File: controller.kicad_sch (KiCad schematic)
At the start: 26 parts, among them U4 STM32H742VGTx

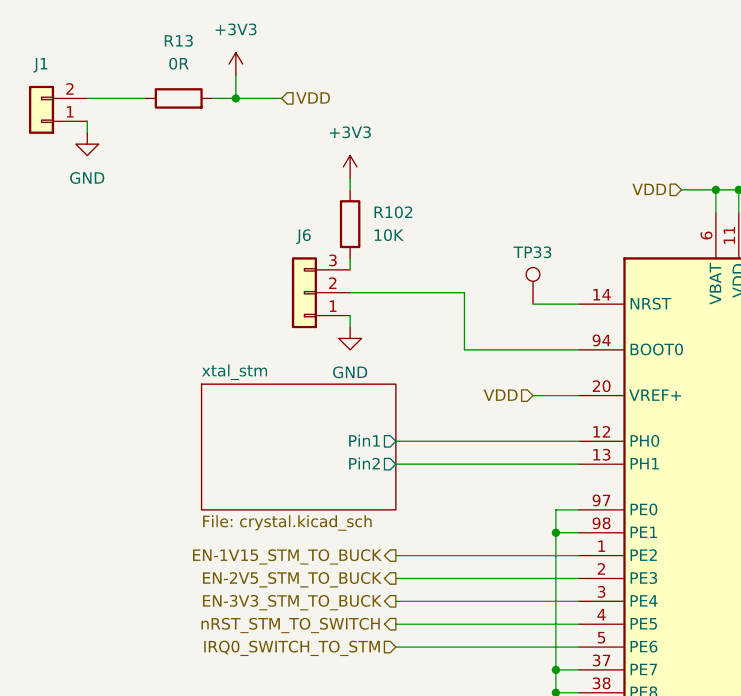
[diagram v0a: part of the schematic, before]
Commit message: moves +3V3 converter to root. Refs: #1
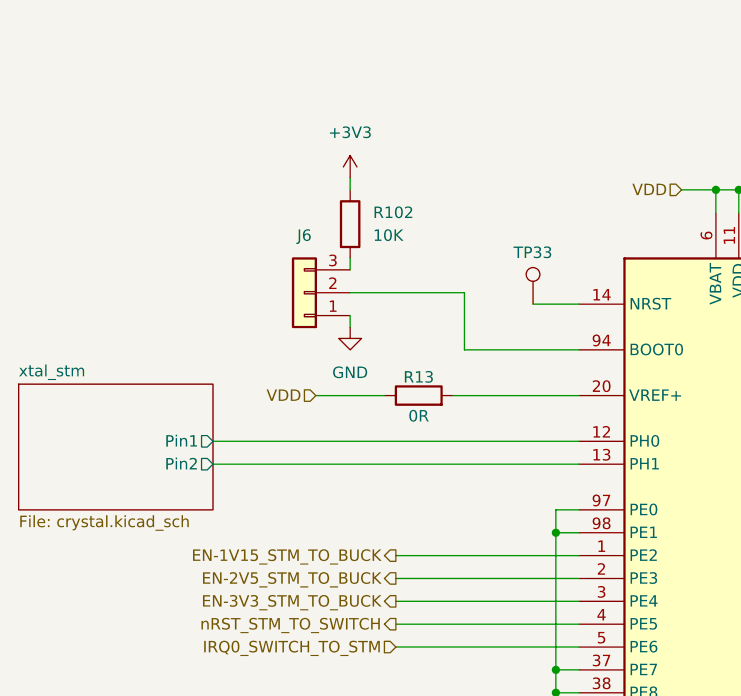
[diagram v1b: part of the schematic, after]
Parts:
- removed J1: ~, KL:02x01_2.54mm_Header, symbol KL_Headers:02x01_2.54mm_Header
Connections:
- net +3V3: no longer C70.1, C75.1, C76.1, C77.1, C78.1, C79.1, C80.1, C85.1, R13.2, U4.100 (VDD), U4.11 (VDD), U4.20 (VREF+), U4.21 (VDDA), U4.27 (VDD), U4.50 (VDD), U4.6 (VBAT), U4.75 (VDD)
- net VDD: now reaches R13.1
- net VDD: now also C70.1, C75.1, C76.1, C77.1, C78.1, C79.1, C80.1, C85.1, U4.100 (VDD), U4.11 (VDD), U4.21 (VDDA), U4.27 (VDD), U4.50 (VDD), U4.6 (VBAT), U4.75 (VDD)
- new net: R13.2, U4.20 (VREF+)
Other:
- moved on the sheet: R13

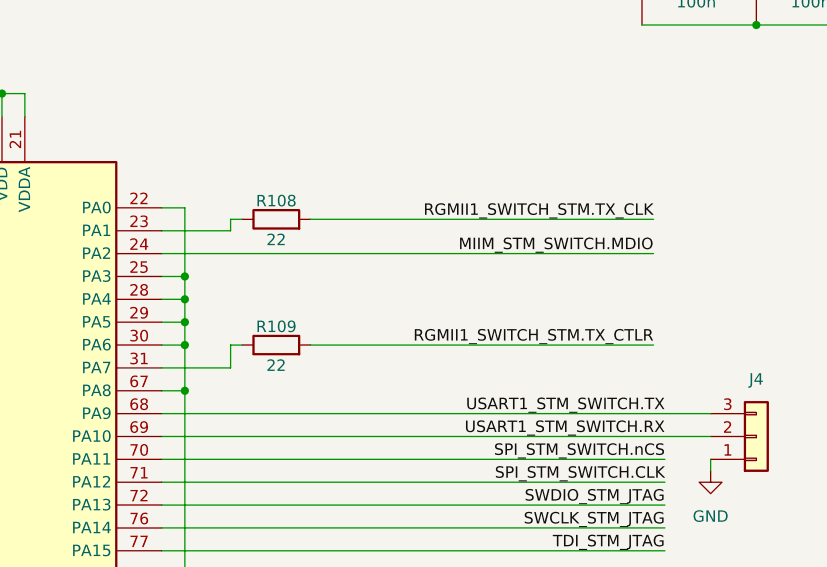
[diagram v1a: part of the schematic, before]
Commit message: fixes RGMII1 TX and RX resistors and duplicate name. Refs: #1
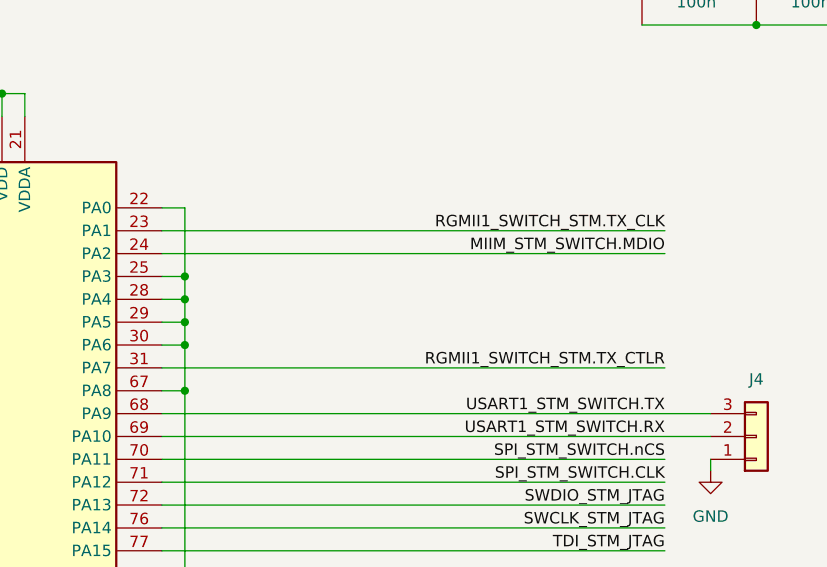
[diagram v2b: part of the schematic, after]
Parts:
- removed R108, R109: 22, KL_Footprints:R_0603, symbol KL_R:R_22_100mW_1pct_0603
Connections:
- net RGMII1_SWITCH_STM.TX_CLK: now also U4.23 (PA1)
- net RGMII1_SWITCH_STM.TX_CTLR: now also U4.31 (PA7)

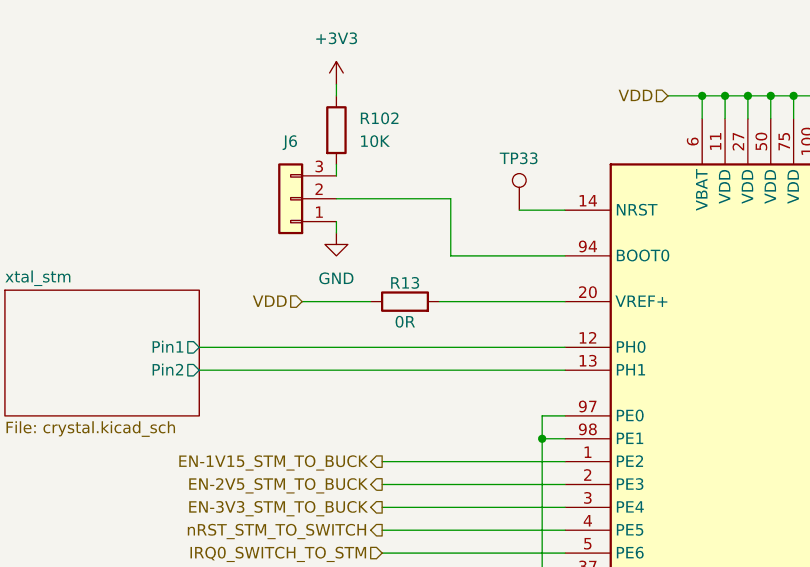
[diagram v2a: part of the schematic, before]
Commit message: fixes duplicate R13. Refs: #1
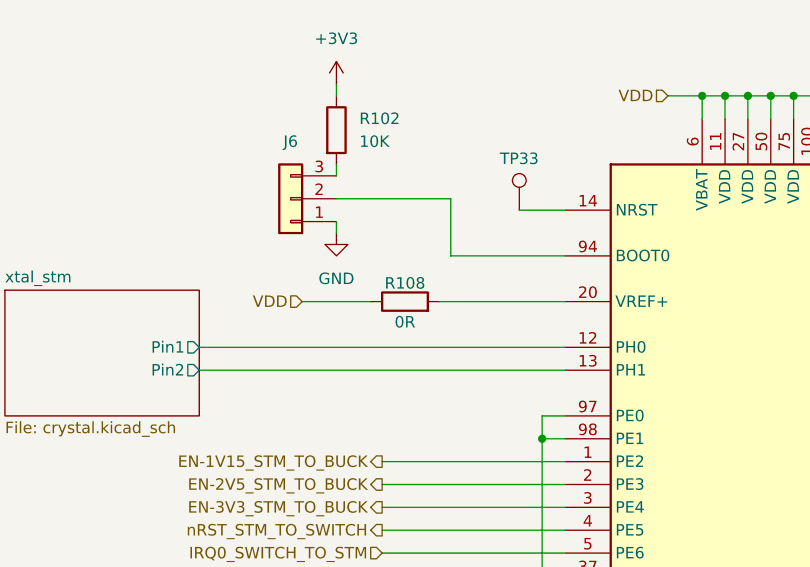
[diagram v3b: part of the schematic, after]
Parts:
- removed R13: 0R, KL_Footprints:R_2512, symbol KL_R:R_0R_2W_5_2512
- added R108: 0R, KL_Footprints:R_2512, symbol KL_R:R_0R_2W_5_2512
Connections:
- net VDD: now also R108.1
- net at U4.20 (VREF+): now also R108.2
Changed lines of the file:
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@@
-	)
-	(symbol
-		(lib_id "KL_R:R_0R_2W_5_2512")
-		(at 60.96 54.61 90)
-		(unit 1)
-		(exclude_from_sim no)
-		(in_bom yes)
-		(on_board yes)
-		(dnp no)
-		(property "Reference" "R13"
-			(at 60.96 52.578 90)
-			(effects
-				(font
-					(size 1.27 1.27)
-				)
-			)
-		)
-		(property "Value" "0R"
-			(at 60.96 56.896 90)
-			(effects
-				(font
-					(size 1.27 1.27)
-				)
-			)
-		)
-		(property "Footprint" "KL_Footprints:R_2512"
-			(at 60.96 56.388 90)
-			(effects
-				(font
-					(size 1.27 1.27)
-				)
-				(hide yes)
-			)
-		)
-		(property "Datasheet" "~"
-			(at 60.96 54.61 0)
-			(effects
-				(font
-					(size 1.27 1.27)
-				)
-				(hide yes)
-			)
-		)
-		(property "Description" "Resistor"
-			(at 60.96 54.61 0)
-			(effects
-				(font
-					(size 1.27 1.27)
-				)
-				(hide yes)
-			)
-		)
-		(property "Power" "2"
-			(at 60.96 54.61 0)
-			(effects
-				(font
-					(size 1.27 1.27)
-				)
-				(hide yes)
-			)
-		)
-		(property "Tolerance" "5"
-			(at 60.96 54.61 0)
-			(effects
-				(font
-					(size 1.27 1.27)
-				)
-				(hide yes)
-			)
-		)
-		(property "Mouser" "652-CRF2512-J-000ELF "
-			(at 60.96 54.61 0)
-			(effects
-				(font
-					(size 1.27 1.27)
-				)
-				(hide yes)
-			)
-		)
-		(property "Digikey" "118-CRF2512-J/-000ELFCT-ND"
-			(at 60.96 54.61 0)
-			(effects
-				(font
-					(size 1.27 1.27)
-				)
-				(hide yes)
-			)
-		)
-		(property "LCSC" "C2778666"
-			(at 60.96 54.61 0)
-			(effects
-				(font
-					(size 1.27 1.27)
-				)
-				(hide yes)
-			)
-		)
-		(pin "2"
-		)
-		(pin "1"
-		)
-		(instances
-			(project ""
-				(path "/d4536448-b109-4159-96e2-3dc21baf2d6e/06488c82-a47f-4277-b0ee-3bd211d8922a"
-					(reference "R13")
-					(unit 1)
-				)
-			)
-		)
 	)
 	(symbol
@@
 					(unit 1)
 				)
+			)
+		)
+	)
+	(symbol
+		(lib_id "KL_R:R_0R_2W_5_2512")
+		(at 60.96 54.61 90)
+		(unit 1)
+		(exclude_from_sim no)
+		(in_bom yes)
+		(on_board yes)
+		(dnp no)
+		(property "Reference" "R108"
+			(at 60.96 52.578 90)
+			(effects
+				(font
+					(size 1.27 1.27)
+				)
+			)
+		)
+		(property "Value" "0R"
+			(at 60.96 56.896 90)
+			(effects
+				(font
+					(size 1.27 1.27)
+				)
+			)
+		)
+		(property "Footprint" "KL_Footprints:R_2512"
+			(at 60.96 56.388 90)
+			(effects
+				(font
+					(size 1.27 1.27)
+				)
+				(hide yes)
+			)
+		)
+		(property "Datasheet" "~"
+			(at 60.96 54.61 0)
+			(effects
+				(font
+					(size 1.27 1.27)
+				)
+				(hide yes)
+			)
+		)
+		(property "Description" "Resistor"
+			(at 60.96 54.61 0)
+			(effects
+				(font
+					(size 1.27 1.27)
+				)
+				(hide yes)
+			)
+		)
+		(property "Power" "2"
+			(at 60.96 54.61 0)
+			(effects
+				(font
+					(size 1.27 1.27)
+				)
+				(hide yes)
+			)
+		)
+		(property "Tolerance" "5"
+			(at 60.96 54.61 0)
+			(effects
+				(font
+					(size 1.27 1.27)
+				)
+				(hide yes)
+			)
+		)
+		(property "Mouser" "652-CRF2512-J-000ELF "
+			(at 60.96 54.61 0)
+			(effects
+				(font
+					(size 1.27 1.27)
+				)
+				(hide yes)
+			)
+		)
+		(property "Digikey" "118-CRF2512-J/-000ELFCT-ND"
+			(at 60.96 54.61 0)
+			(effects
+				(font
+					(size 1.27 1.27)
+				)
+				(hide yes)
+			)
+		)
+		(property "LCSC" "C2778666"
+			(at 60.96 54.61 0)
+			(effects
+				(font
+					(size 1.27 1.27)
+				)
+				(hide yes)
+			)
+		)
+		(pin "2"
+		)
+		(pin "1"
+		)
+		(instances
+			(project "shish-lan"
+				(path "/d4536448-b109-4159-96e2-3dc21baf2d6e/06488c82-a47f-4277-b0ee-3bd211d8922a"
+					(reference "R108")
+					(unit 1)
+				)

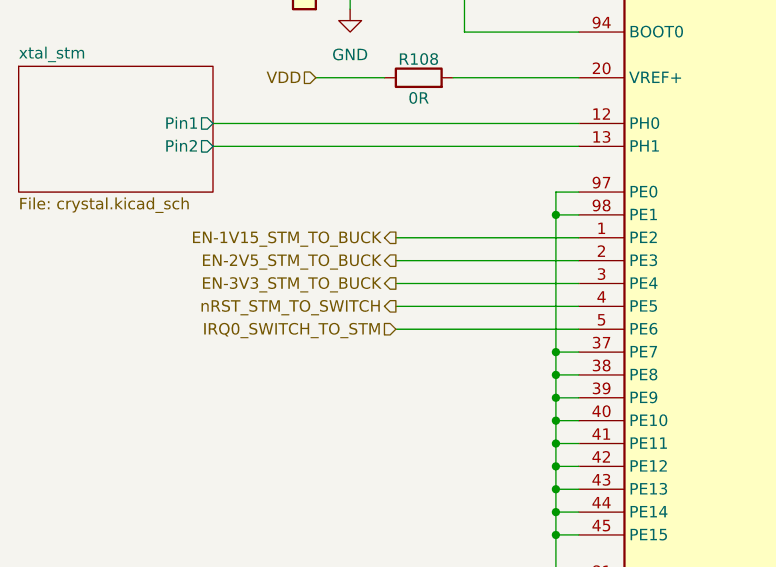
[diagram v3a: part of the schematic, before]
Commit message: removes unused en-3v3 signal from STM. Refs: #1
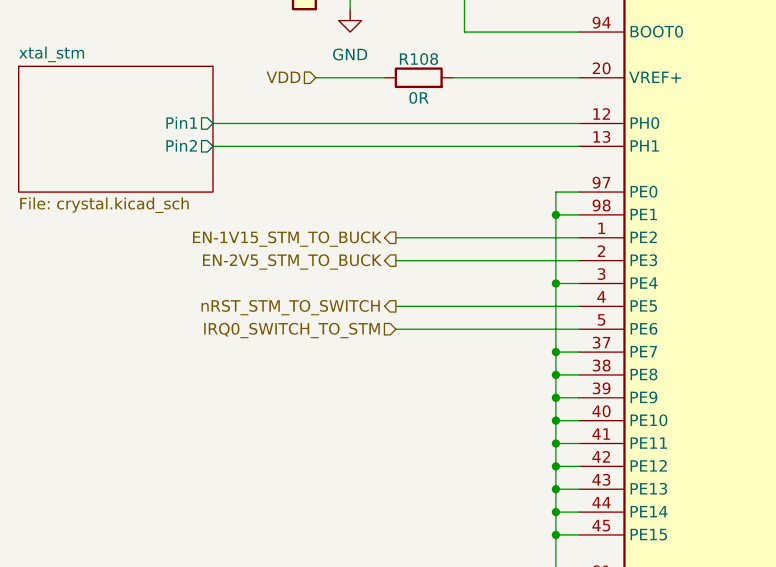
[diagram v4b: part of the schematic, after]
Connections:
- net EN-3V3_STM_TO_BUCK is gone; now on net GND: U4.3 (PE4)
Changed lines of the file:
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@@
 	)
 	(junction
+		(at 76.2 77.47)
+		(diameter 0)
+		(color 0 0 0 0)
+	)
+	(junction
 		(at 91.44 181.61)
 		(diameter 0)
@@
 	(wire
 		(pts
-			(xy 76.2 69.85) (xy 76.2 85.09)
+			(xy 76.2 69.85) (xy 76.2 77.47)
 		)
 		(stroke
@@
 	(wire
 		(pts
+			(xy 76.2 77.47) (xy 76.2 85.09)
+		)
+		(stroke
+			(width 0)
+			(type default)
+		)
+	)
+	(wire
+		(pts
 			(xy 124.46 113.03) (xy 127 113.03)
 		)
@@
 	(wire
 		(pts
+			(xy 76.2 77.47) (xy 78.74 77.47)
+		)
+		(stroke
+			(width 0)
+			(type default)
+		)
+	)
+	(wire
+		(pts
 			(xy 127 168.91) (xy 124.46 168.91)
 		)
@@
 		)
 	)
-	(wire
-		(pts
-			(xy 58.42 77.47) (xy 78.74 77.47)
-		)
-		(stroke
-			(width 0)
-			(type default)
-		)
-	)
 	(bus
 		(pts
@@
 		(effects
 			(font
-				(size 1.27 1.27)
-			)
-			(justify right)
-		)
-	)
-	(hierarchical_label "EN-3V3_STM_TO_BUCK"
-		(shape output)
-		(at 58.42 77.47 180)
-		(effects
-			(font

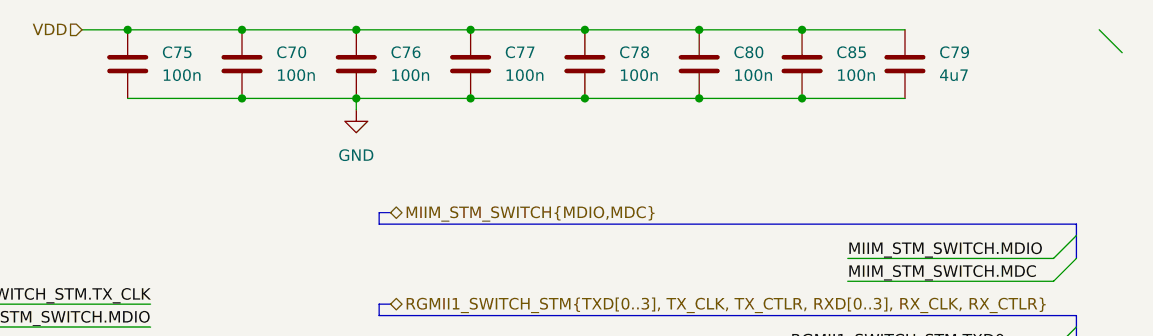
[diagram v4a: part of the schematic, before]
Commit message: fixes duplicate buffer caps for STM. Refs: #1
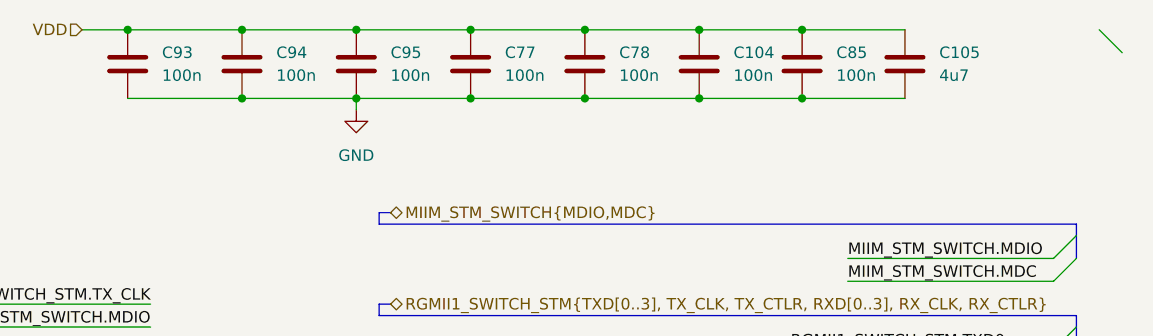
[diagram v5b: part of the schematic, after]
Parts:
- removed C70, C75, C76, C80: 100n, KL_Footprints:C_0603, symbol KL_C:C_100n_10V_10_X7R_0603
- removed C79: 4u7, KL_Footprints:C_0603, symbol KL_C:C_4u7_10V_10_X5R_0603
- added C104, C93, C94, C95: 100n, KL_Footprints:C_0603, symbol KL_C:C_100n_10V_10_X7R_0603
- added C105: 4u7, KL_Footprints:C_0603, symbol KL_C:C_4u7_10V_10_X5R_0603
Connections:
- net GND: now also C104.2, C105.2, C93.2, C94.2, C95.2
- net VDD: now also C104.1, C105.1, C93.1, C94.1, C95.1

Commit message: fixes ERC errors in DC/DC converters
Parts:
- R102: footprint KL_Footprints:C_0603 -> KL_Footprints:R_0603
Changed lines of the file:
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@@
 			)
 		)
-		(property "Footprint" "KL_Footprints:C_0603"
+		(property "Footprint" "KL_Footprints:R_0603"
 			(at 51.562 35.56 90)
 			(effects

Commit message: updates pin headers
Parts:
- J4, J6: footprint KL:03x01_2.54mm_Header -> KL_Footprints:03x01_2.54mm_Header
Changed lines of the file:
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@@
 		(dnp no)
 		(property "Reference" "J4"
-			(at 190.5 63.5 0)
+			(at 190.246 74.676 0)
 			(effects
 				(font
@@
 			)
 		)
-		(property "Footprint" "KL:03x01_2.54mm_Header"
+		(property "Footprint" "KL_Footprints:03x01_2.54mm_Header"
 			(at 191.262 78.232 0)
 			(effects
@@
 			)
 		)
-		(property "Footprint" "KL:03x01_2.54mm_Header"
+		(property "Footprint" "KL_Footprints:03x01_2.54mm_Header"
 			(at 47.498 51.562 0)
 			(effects
